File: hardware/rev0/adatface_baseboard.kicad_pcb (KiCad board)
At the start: 4 copper layers, 123 x 111.6 mm, 90 parts, among them J1 Conn_01x06_Male, J2 Conn_02x32_Odd_Even, J3 Conn_02x32_Odd_Even, J4 Connector_USB_C_Receptacle_US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, J5 Connector_USB_C_Receptacle_US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, J6 Conn_01x06_Male, J7 Conn_01x26_Male, J8 Conn_01x01_Male, J9 Conn_01x01_Male, U1 PLR135-T10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

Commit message: hardware: fix header width and 3d model paths
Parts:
- moved H4 3.74 mm to (121.8, 112.6)
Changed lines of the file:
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@@
   )
   (footprint "MountingHole:MountingHole_3.2mm_M3_Pad_Via" (layer "F.Cu")
-    (at 122.936 116.205)
+    (at 121.793 112.649)
     (descr "Mounting Hole 3.2mm, M3")
     (tags "mounting hole 3.2mm m3")

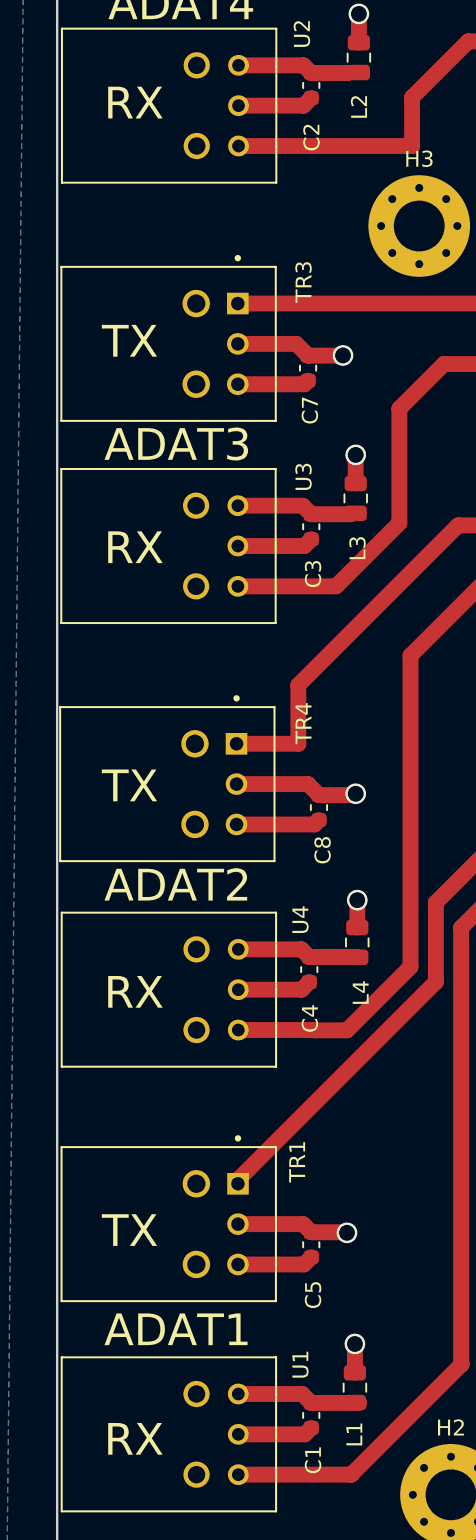
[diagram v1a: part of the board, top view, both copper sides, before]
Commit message: Fix missing symbol and footprint libraries for toslink
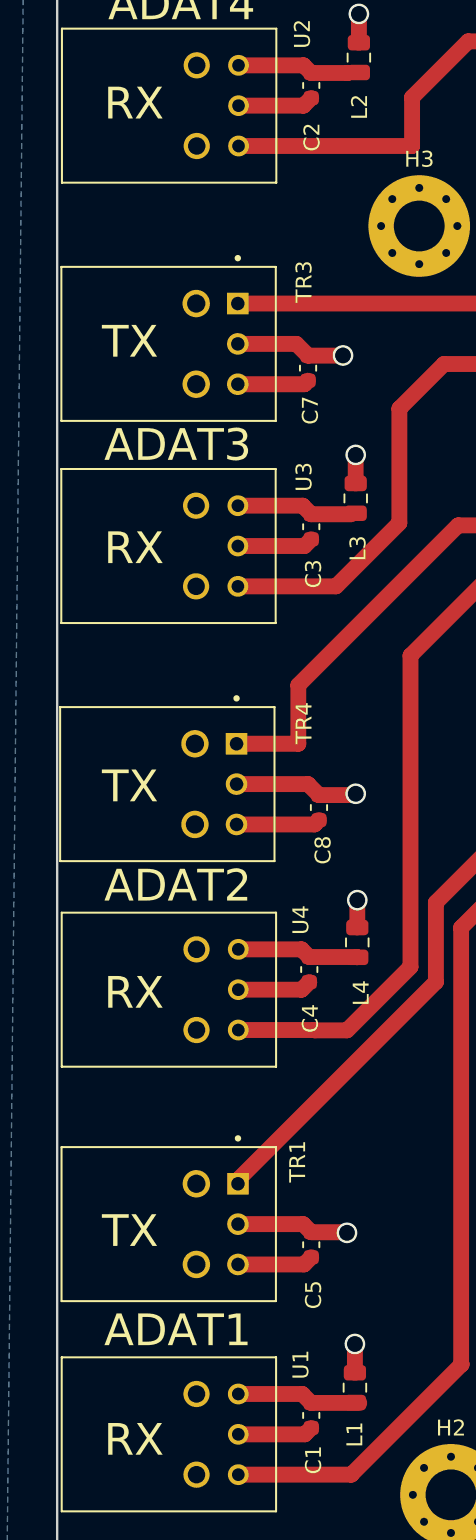
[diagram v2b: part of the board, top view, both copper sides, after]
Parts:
- TR1, TR2, TR3, TR4: footprint toslink:T10W -> toslink:PLT133_T10W

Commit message: change toslink footprints to T8 variation
Footprint is the same except for the edition of NPTH for
plastic mounting feet, so either T8 or T10 versions can
be used.
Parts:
- TR1, TR2, TR3, TR4: value PLT133_T10W -> PLT133_T8; footprint toslink:PLT133_T10W -> toslink:PLT133_T8
- U1, U2, U3, U4: value PLR135-T10 -> PLR135_T8; footprint toslink:PLR135-T10_PLT133-T10W -> toslink:PLR135-T8_PLT133-T8
